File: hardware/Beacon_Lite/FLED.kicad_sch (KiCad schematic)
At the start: 2 parts, among them U4 IS31FL3741

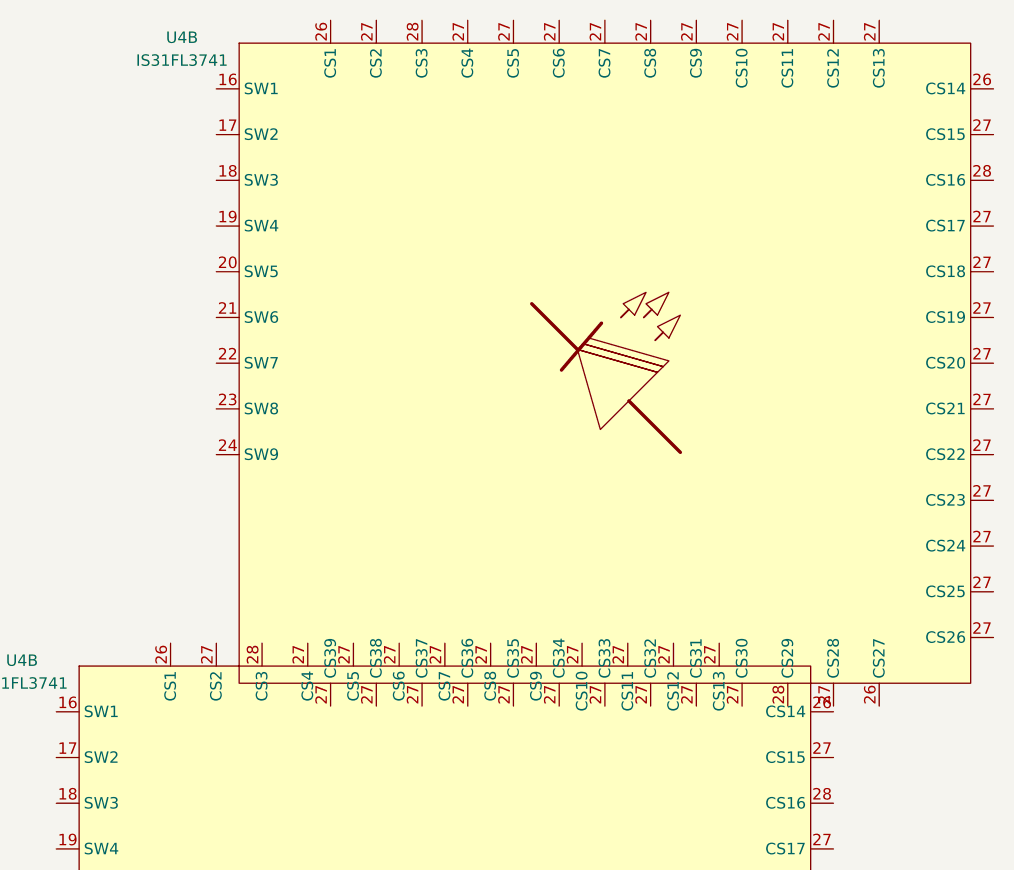
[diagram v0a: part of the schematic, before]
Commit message: Started ST project. Create sch symbols.
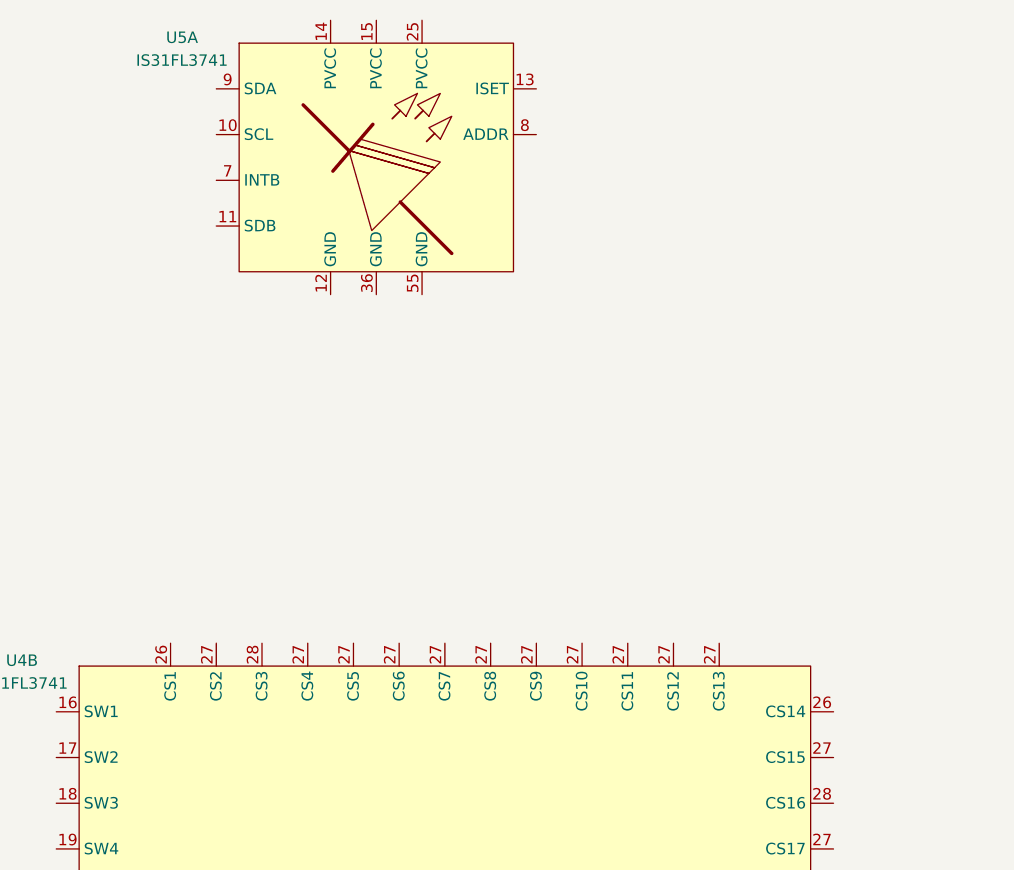
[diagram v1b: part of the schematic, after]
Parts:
- renumbered U4 to U5

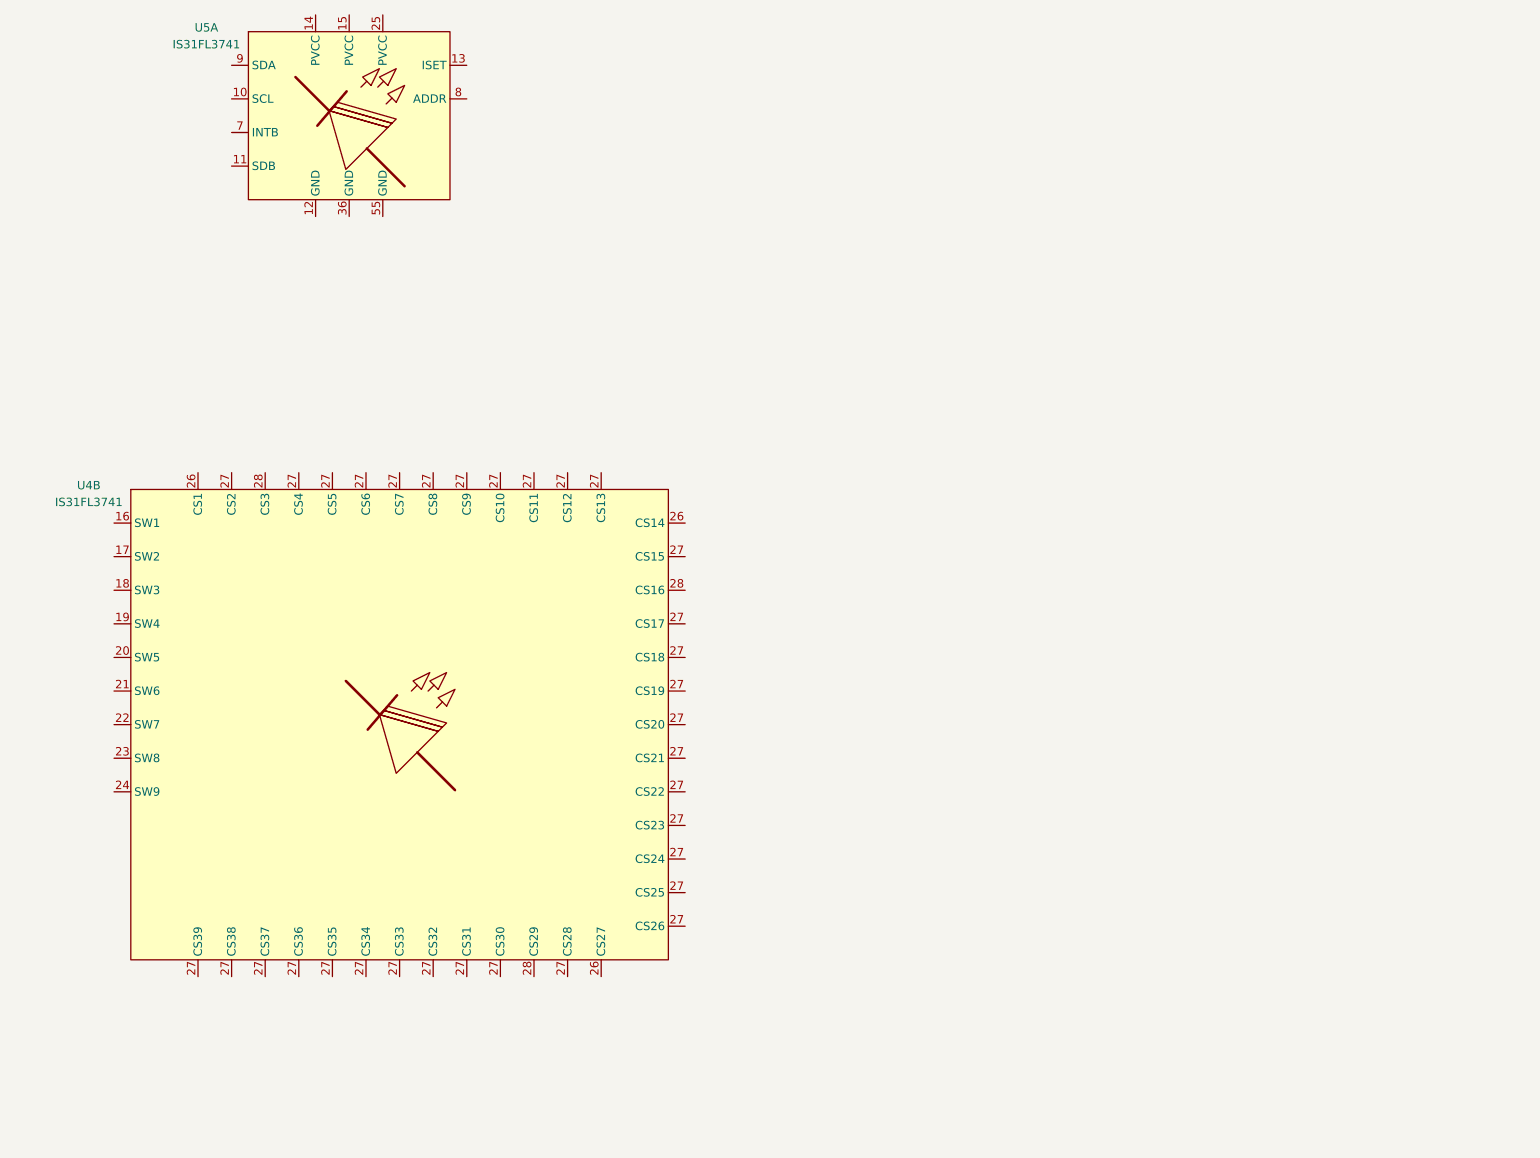
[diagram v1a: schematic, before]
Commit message: Minor schematic and symbol updates
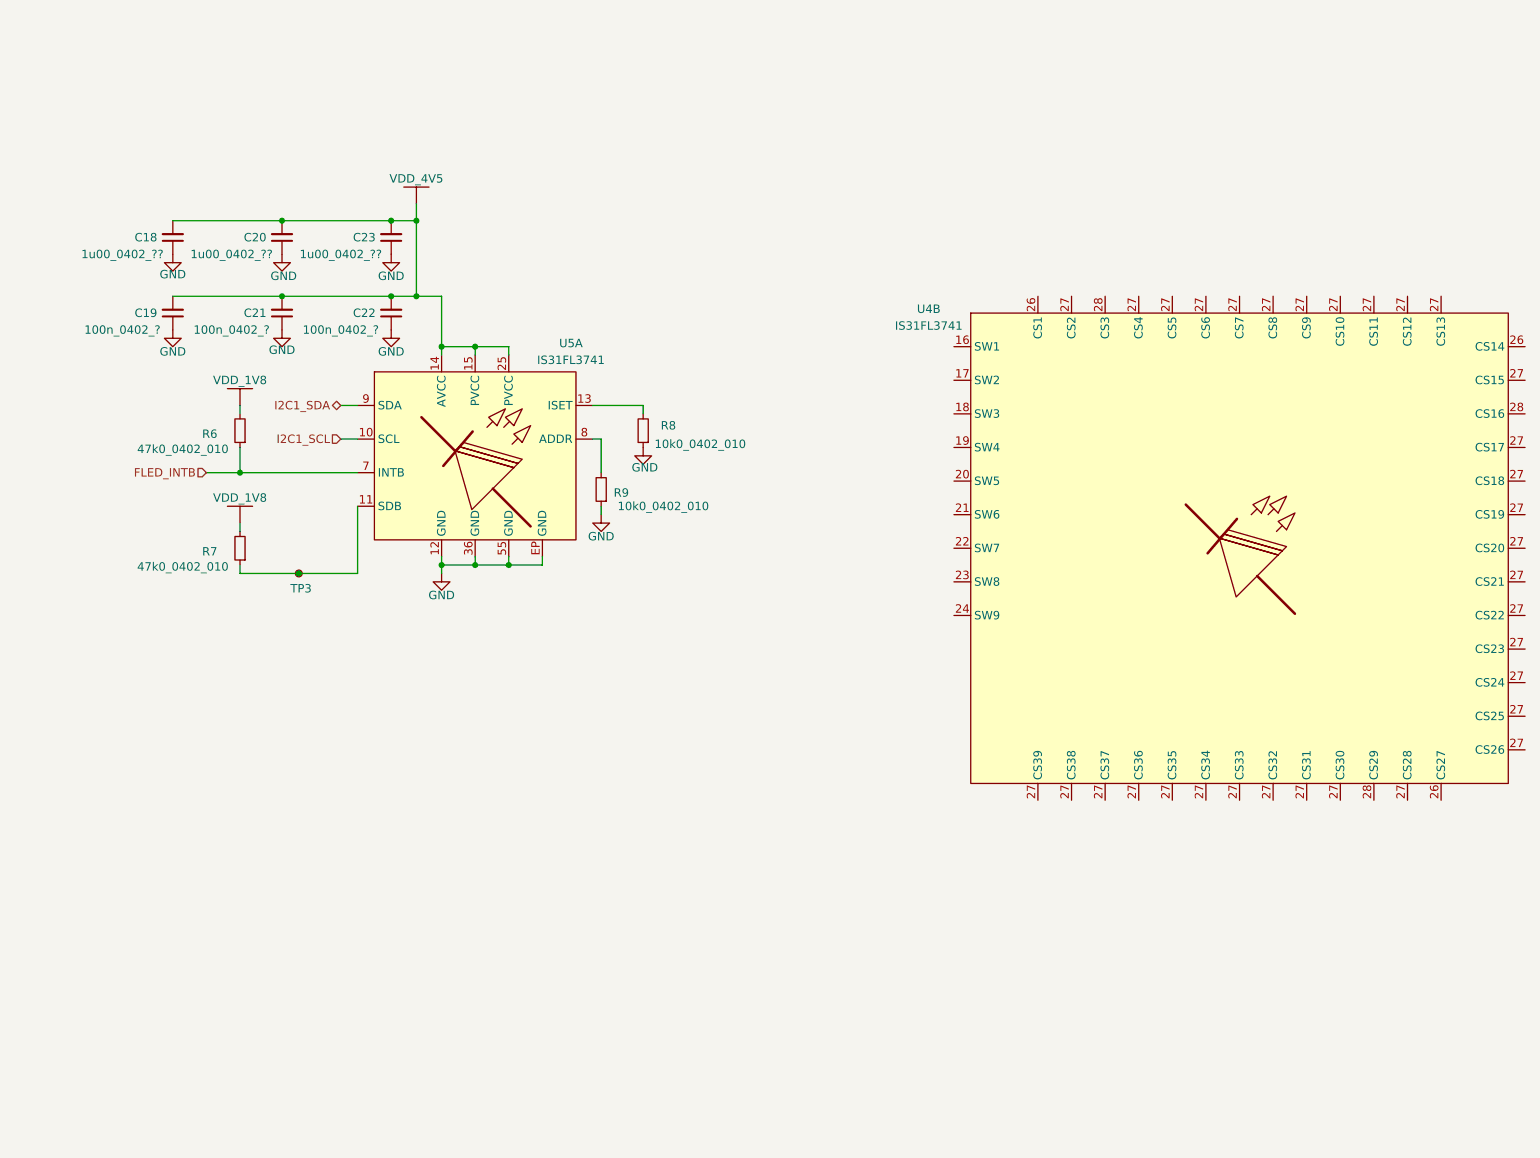
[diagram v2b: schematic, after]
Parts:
- added C18, C20, C23: 1u00_0402_??, Footprint_Library:0402_1005Metric_Handsolder, symbol Device:C_Small
- added C19, C21, C22: 100n_0402_?, Footprint_Library:0402_1005Metric_Handsolder, symbol Device:C_Small
- added R6, R7: 47k0_0402_010, Footprint_Library:0402_1005Metric_Handsolder, symbol Device:R_Small
- added R8, R9: 10k0_0402_010, Footprint_Library:0402_1005Metric_Handsolder, symbol Device:R_Small
- added TP3: TestPoint_Small, symbol Connector:TestPoint_Small
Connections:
- net I2C1_SCL: now reaches U5.10 (SCL)
- net at U5.11 (SDB): now also R7.1, TP3.1
- net GND: now reaches U5.12 (GND)
- net GND: now also U5.36 (GND), U5.55 (GND), U5.EP (GND), C18.1, C19.1, C20.1, C21.1, C22.1, C23.1, R8.1, R9.1
- net at U5.13 (ISET): now also R8.2
- net VDD_4V5: now reaches U5.14 (AVCC)
- net VDD_4V5: now also U5.15 (PVCC), U5.25 (PVCC), C18.2, C19.2, C20.2, C21.2, C22.2, C23.2
- net FLED_INTB: now reaches U5.7 (INTB)
- net FLED_INTB: now also R6.1
- net at U5.8 (ADDR): now also R9.2
- net I2C1_SDA: now reaches U5.9 (SDA)
- new net VDD_1V8: R6.2, R7.2
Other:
- moved on the sheet: U4B

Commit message: Started programming NUCLEO-H533 in VSCODE
* Able to use C++ and C
* Successful able to debug
* Can blink an LED when button is pressed via an interrupt.
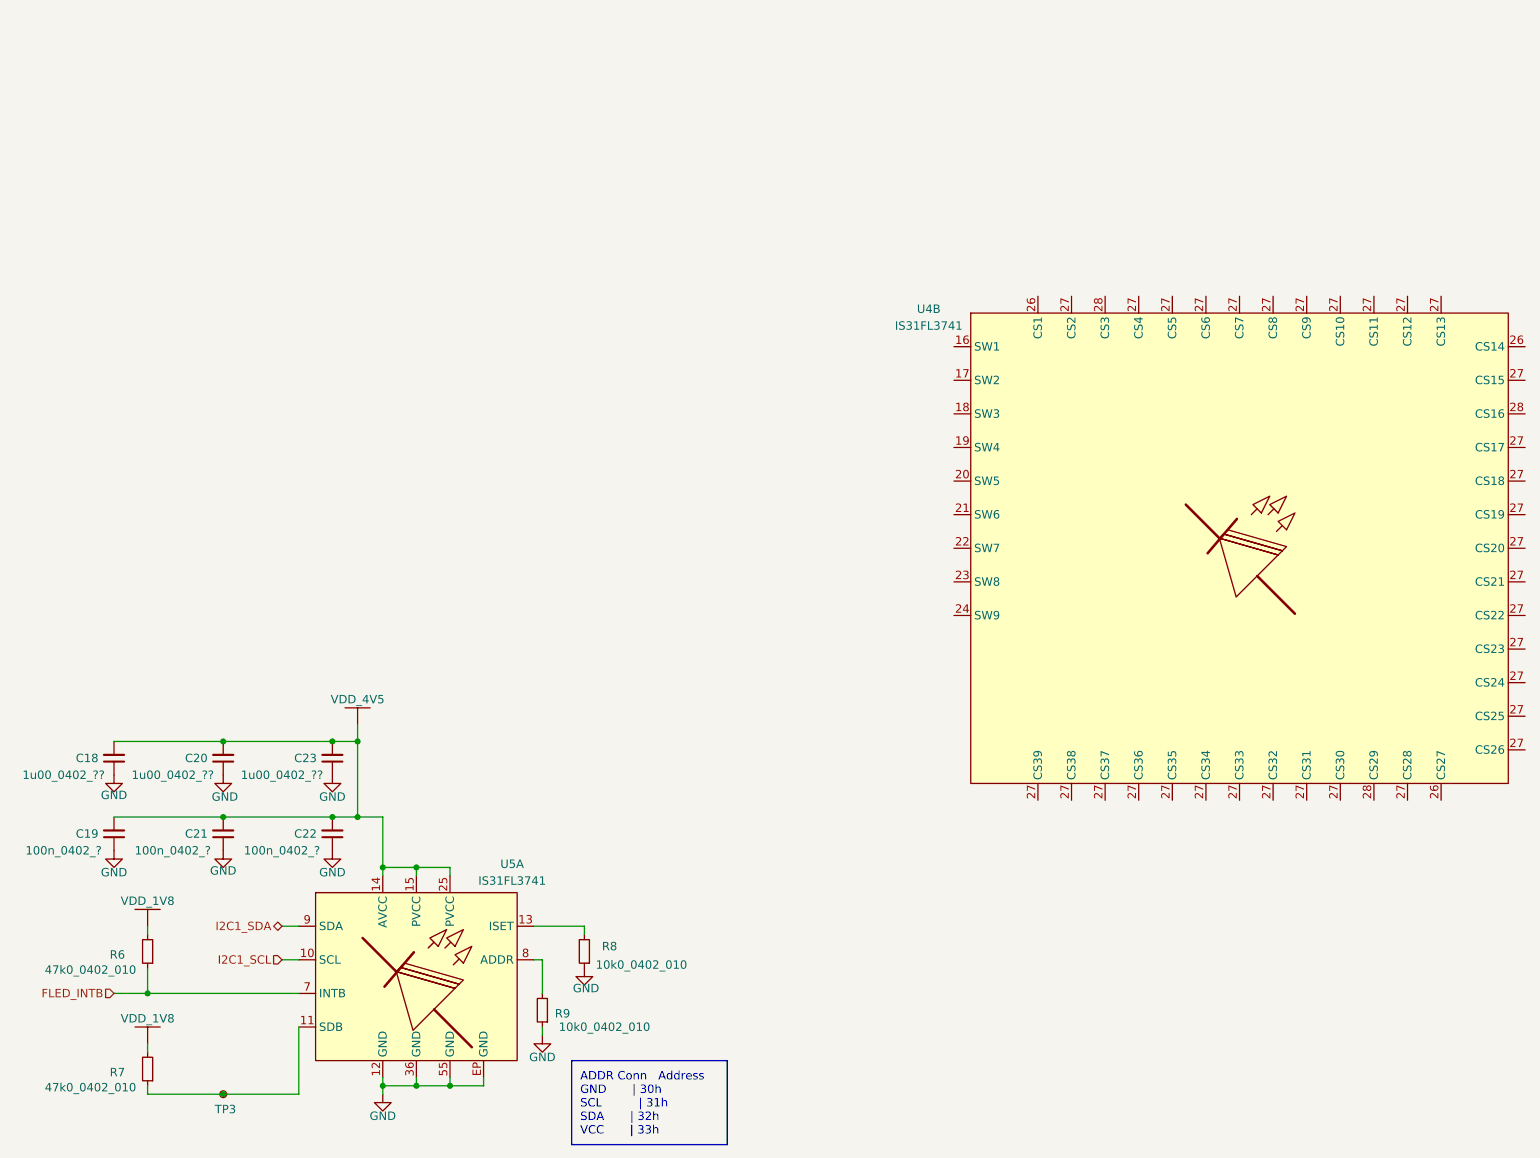
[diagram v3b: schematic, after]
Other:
- note added: "ADDR Conn Address GND | 30h SCL | 31h SDA | 32h VCC | 33h"
- moved on the sheet: C18, C19, C20, C21, C22, C23, R6, R7, R8, R9, TP3, U5A
